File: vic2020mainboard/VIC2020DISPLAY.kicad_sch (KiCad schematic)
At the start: 16 parts, among them J3 FONT SELECT, J5 SVIDEO Out, J6 Audio Out, J7 Video Out, U14 74LS245, U15 74LS245, U16 74LS245, U17 AS6C1008-55PCN, U18 74LS245, U19 2764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

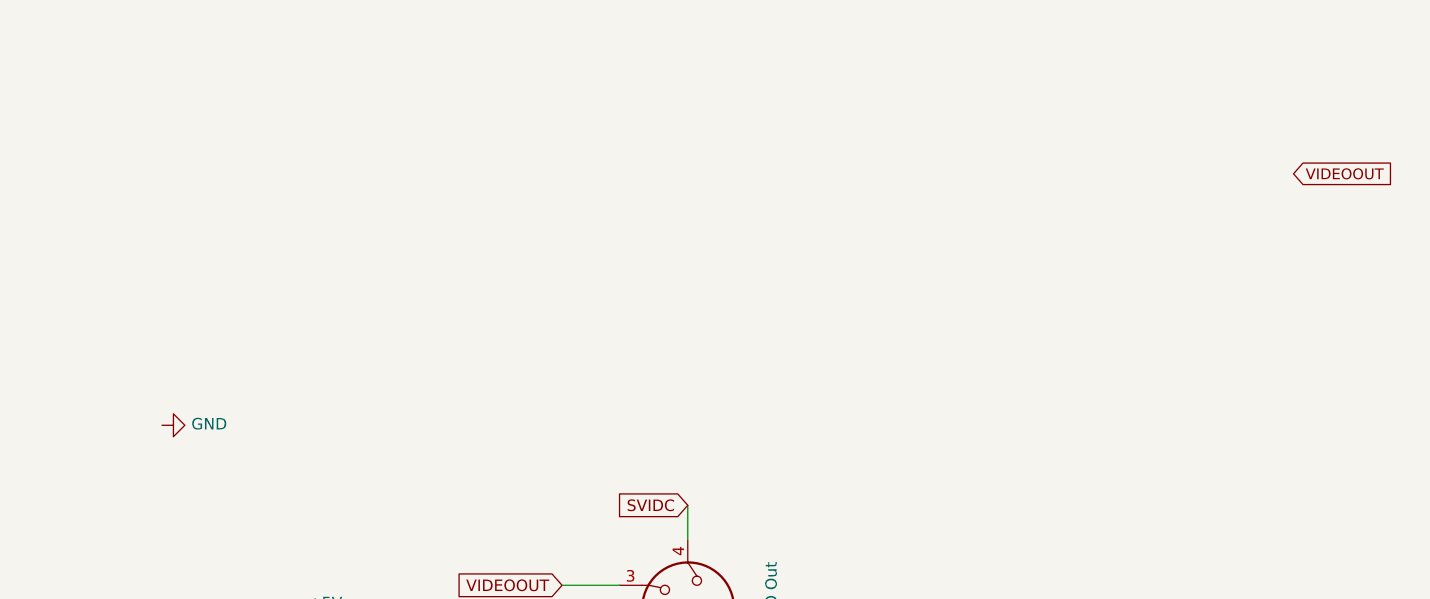
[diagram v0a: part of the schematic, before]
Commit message: Added power supply circuit for 9V AC input
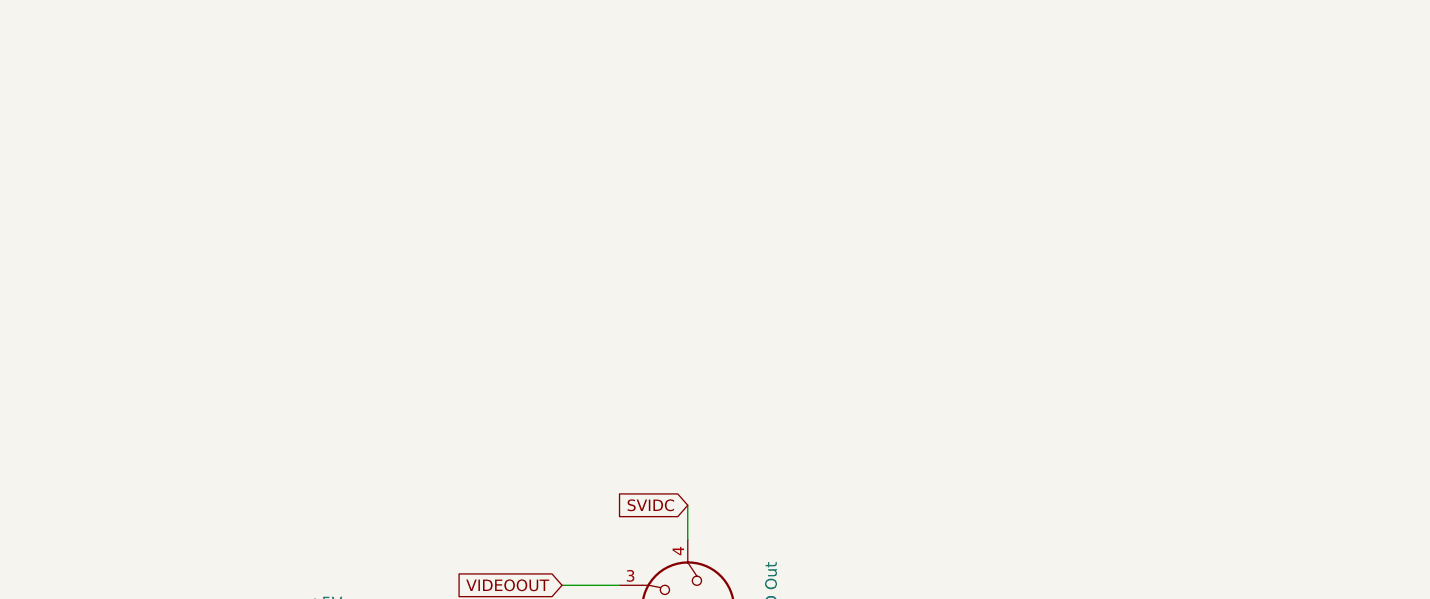
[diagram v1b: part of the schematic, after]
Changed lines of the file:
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@@
 		)
 	)
-	(global_label "VIDEOOUT"
-		(shape input)
-		(at 273.05 74.93 0)
-		(effects
-			(font
-				(size 1.1938 1.1938)
-			)
-			(justify left)
-		)
-		(property "Intersheetrefs" "${INTERSHEET_REFS}"
-			(at 273.05 74.93 0)
-			(hide yes)
-			(show_name no)
-			(do_not_autoplace no)
-			(effects
-				(font
-					(size 1.27 1.27)
-				)
-			)
-		)
-	)
 	(global_label "BD4"
 		(shape input)
@@
 					(unit 1)
 				)
-			)
-		)
-	)
-	(symbol
-		(lib_id "power:GND")
-		(at 147.32 102.87 90)
-		(unit 1)
-		(body_style 1)
-		(exclude_from_sim no)
-		(in_bom yes)
-		(on_board yes)
-		(in_pos_files yes)
-		(dnp no)
-		(property "Reference" "#PWR0157"
-			(at 153.67 102.87 0)
-			(hide yes)
-			(show_name no)
-			(do_not_autoplace no)
-			(effects
-				(font
-					(size 1.27 1.27)
-				)
-			)
-		)
-		(property "Value" "GND"
-			(at 150.5712 102.743 90)
-			(show_name no)
-			(do_not_autoplace no)
-			(effects
-				(font
-					(size 1.27 1.27)
-				)
-				(justify right)
-			)
-		)
-		(property "Footprint" ""
-			(at 147.32 102.87 0)
-			(hide yes)
-			(show_name no)
-			(do_not_autoplace no)
-			(effects
-				(font
-					(size 1.27 1.27)
-				)
-			)
-		)
-		(property "Datasheet" ""
-			(at 147.32 102.87 0)
-			(hide yes)
-			(show_name no)
-			(do_not_autoplace no)
-			(effects
-				(font
-					(size 1.27 1.27)
-				)
-			)
-		)
-		(property "Description" ""
-			(at 147.32 102.87 0)
-			(show_name no)
-			(do_not_autoplace no)
-			(effects
-				(font
-					(size 1.27 1.27)
-				)
-			)
-		)
-		(pin "1"
-		)
-		(instances
-			(project "Vic2020mainboard"
-				(path "/f98df84e-f5f2-4c35-84be-6093352134d0/00000000-0000-0000-0000-00005f5bc33e"
-					(reference "#PWR0157")
-					(unit 1)
-				)
